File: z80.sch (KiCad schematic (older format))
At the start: 6 parts, among them P1 CONN_01X04, U1001 Z8400, U1002 AT28C64B, U1003 AS6C1008, U1004 Z8420, U1005 74LS138

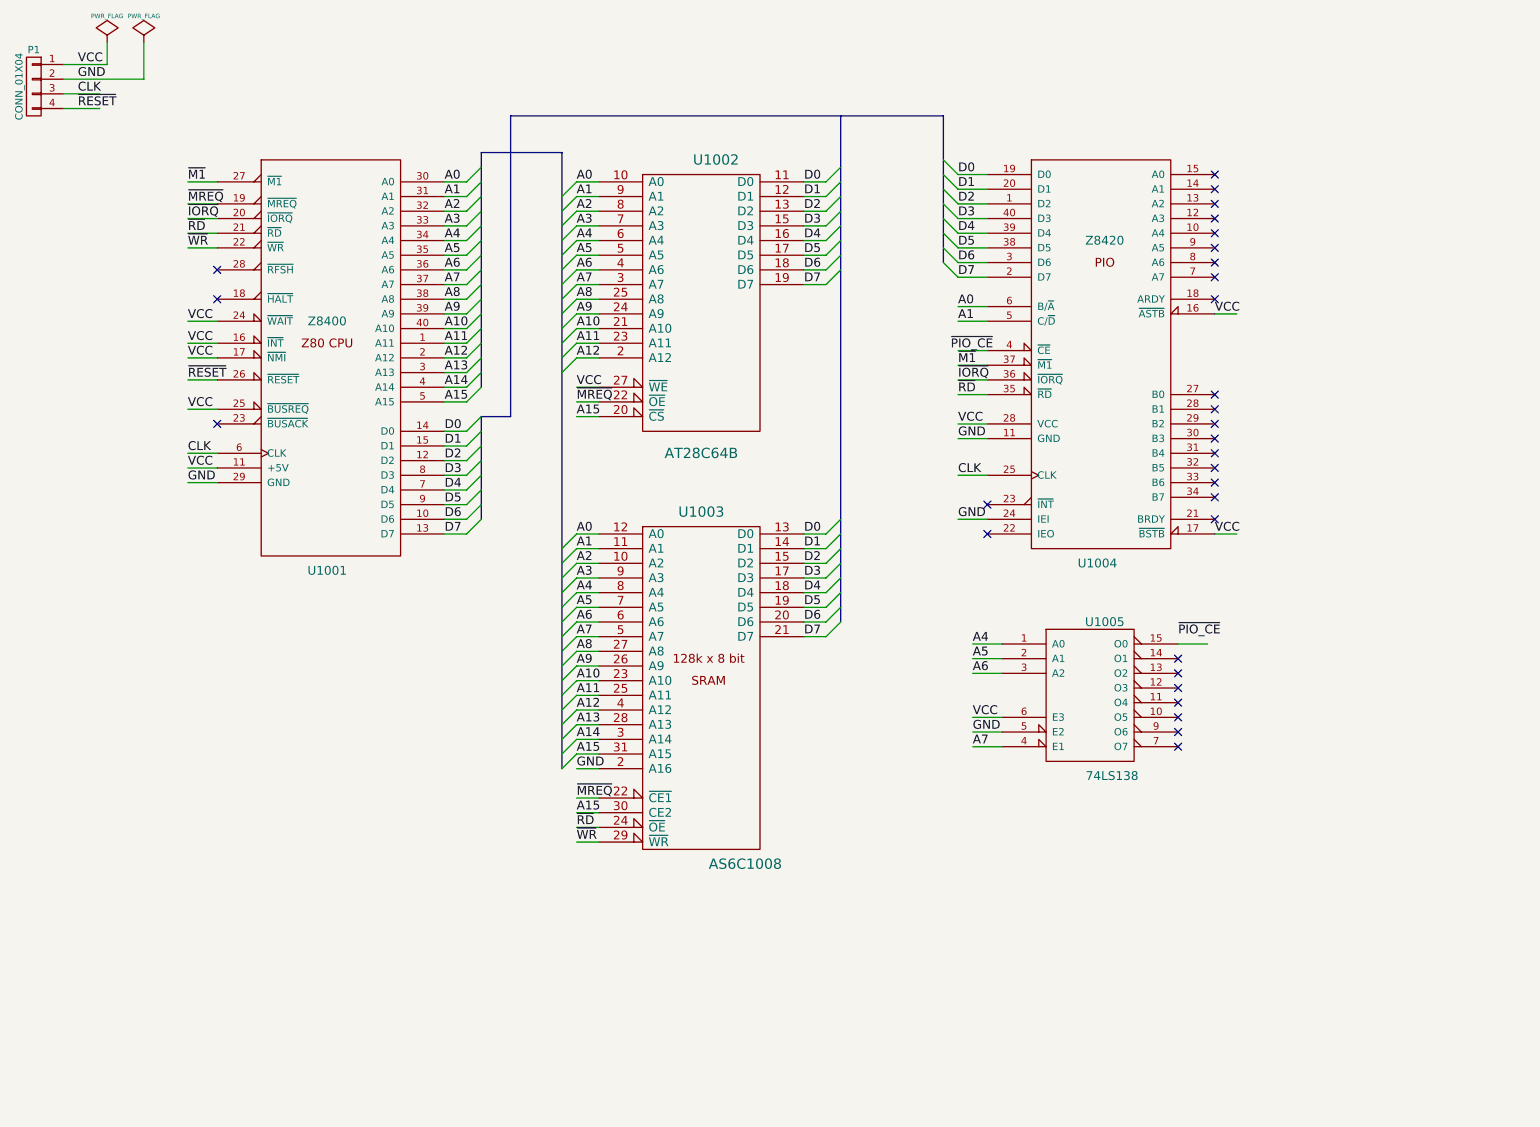
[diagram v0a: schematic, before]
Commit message: Connect ~RESET to the PIO
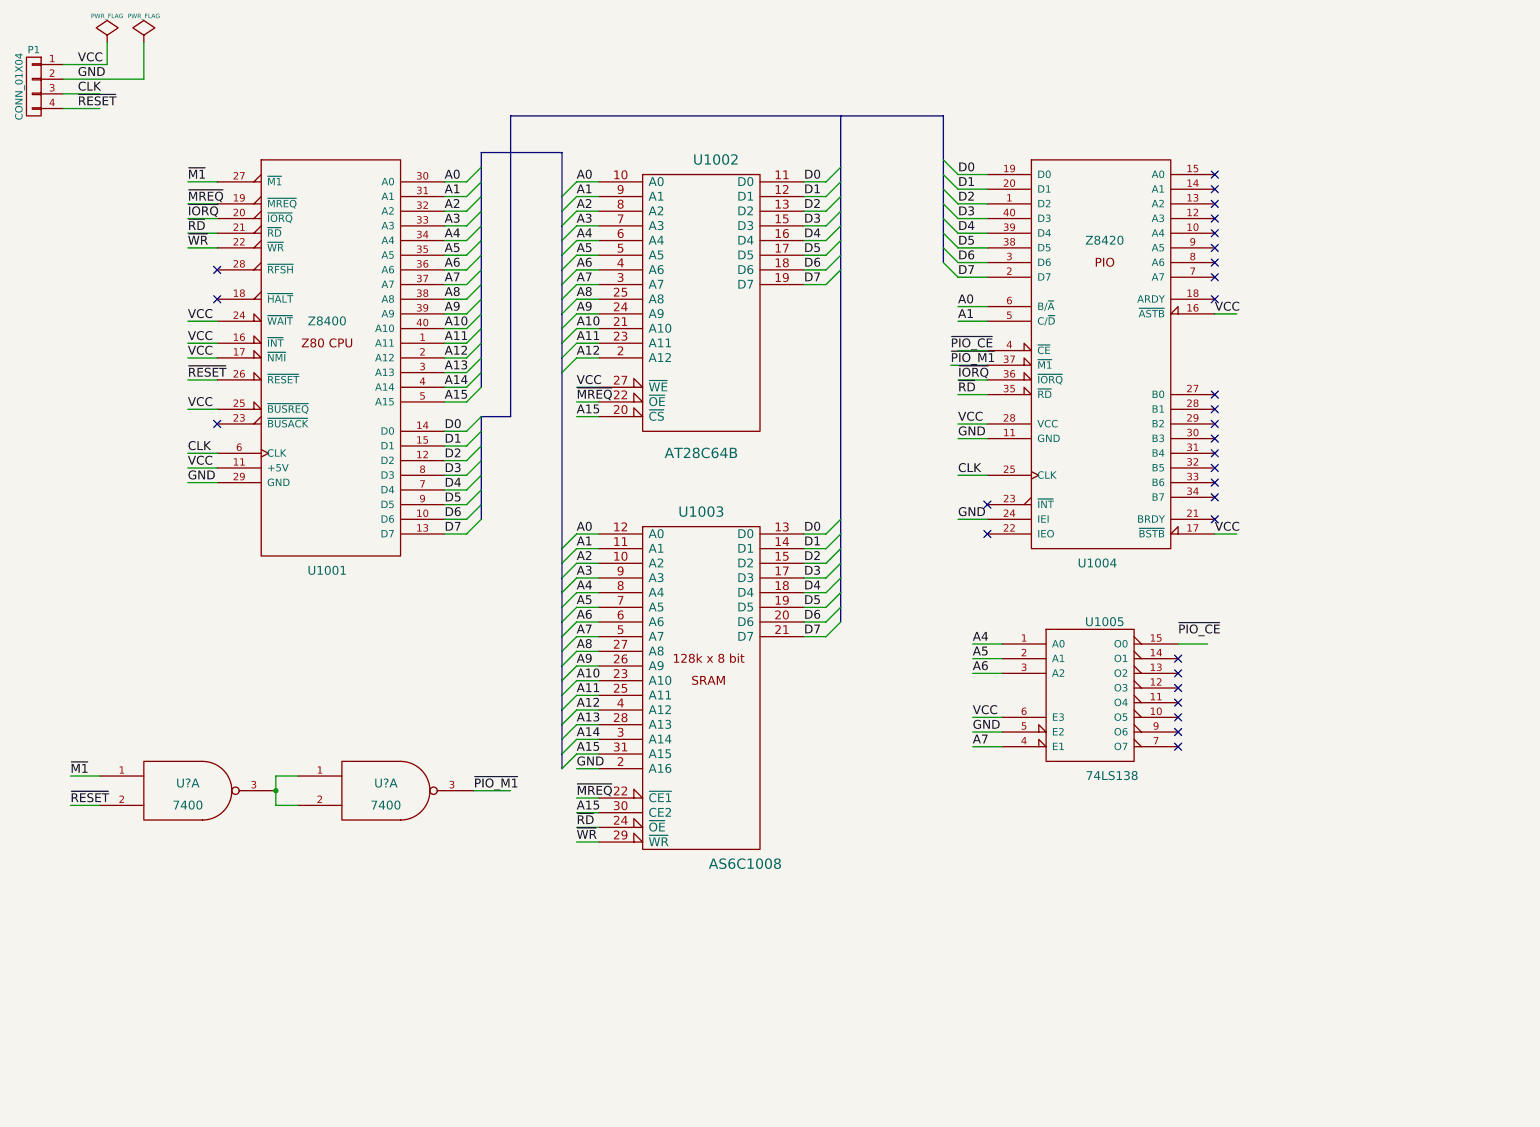
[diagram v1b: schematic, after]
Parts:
- added U? (x2): 7400, symbol 7400
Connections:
- net labels added: ~PIO_M1
- wire segments 123 -> 130
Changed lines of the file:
@@
 Text Label 4500 3100 0    60   ~ 0
 VCC
-Text Label 7100 2950 0    60   ~ 0
-~M1
+Text Label 7050 2950 0    60   ~ 0
+~PIO_M1
 Text Label 4500 3300 0    60   ~ 0
 A15
@@
 	3600 4100 3750 4100
 Wire Bus Line
-	3850 1500 3850 3100
+	3850 1500 3850 1600
+Wire Bus Line
+	3850 1600 3850 1700
+Wire Bus Line
+	3850 1700 3850 1800
+Wire Bus Line
+	3850 1800 3850 1900
+Wire Bus Line
+	3850 1900 3850 2000
+Wire Bus Line
+	3850 2000 3850 2100
+Wire Bus Line
+	3850 2100 3850 2200
+Wire Bus Line
+	3850 2200 3850 2300
+Wire Bus Line
+	3850 2300 3850 2400
+Wire Bus Line
+	3850 2400 3850 2500
+Wire Bus Line
+	3850 2500 3850 2600
+Wire Bus Line
+	3850 2600 3850 2700
+Wire Bus Line
+	3850 2700 3850 2800
+Wire Bus Line
+	3850 2800 3850 2900
+Wire Bus Line
+	3850 2900 3850 3000
+Wire Bus Line
+	3850 3000 3850 3100
 Wire Bus Line
 	3850 1500 4400 1500
@@
 	4650 5600 4500 5600
 Wire Bus Line
-	4400 1500 4400 5700
-Wire Bus Line
-	6300 1250 6300 4700
-Wire Wire Line
-	7100 2950 7300 2950
+	4400 1500 4400 1800
+Wire Bus Line
+	4400 1800 4400 1900
+Wire Bus Line
+	4400 1900 4400 2000
+Wire Bus Line
+	4400 2000 4400 2100
+Wire Bus Line
+	4400 2100 4400 2200
+Wire Bus Line
+	4400 2200 4400 2300
+Wire Bus Line
+	4400 2300 4400 2400
+Wire Bus Line
+	4400 2400 4400 2500
+Wire Bus Line
+	4400 2500 4400 2600
+Wire Bus Line
+	4400 2600 4400 2700
+Wire Bus Line
+	4400 2700 4400 2800
+Wire Bus Line
+	4400 2800 4400 2900
+Wire Bus Line
+	4400 2900 4400 3000
+Wire Bus Line
+	4400 3000 4400 4200
+Wire Bus Line
+	4400 4200 4400 4300
+Wire Bus Line
+	4400 4300 4400 4400
+Wire Bus Line
+	4400 4400 4400 4500
+Wire Bus Line
+	4400 4500 4400 4600
+Wire Bus Line
+	4400 4600 4400 4700
+Wire Bus Line
+	4400 4700 4400 4800
+Wire Bus Line
+	4400 4800 4400 4900
+Wire Bus Line
+	4400 4900 4400 5000
+Wire Bus Line
+	4400 5000 4400 5100
+Wire Bus Line
+	4400 5100 4400 5200
+Wire Bus Line
+	4400 5200 4400 5300
+Wire Bus Line
+	4400 5300 4400 5400
+Wire Bus Line
+	4400 5400 4400 5500
+Wire Bus Line
+	4400 5500 4400 5600
+Wire Bus Line
+	4400 5600 4400 5700
+Wire Bus Line
+	6300 1250 6300 1600
+Wire Bus Line
+	6300 1600 6300 1700
+Wire Bus Line
+	6300 1700 6300 1800
+Wire Bus Line
+	6300 1800 6300 1900
+Wire Bus Line
+	6300 1900 6300 2000
+Wire Bus Line
+	6300 2000 6300 2100
+Wire Bus Line
+	6300 2100 6300 2200
+Wire Bus Line
+	6300 2200 6300 2300
+Wire Bus Line
+	6300 2300 6300 4000
+Wire Bus Line
+	6300 4000 6300 4100
+Wire Bus Line
+	6300 4100 6300 4200
+Wire Bus Line
+	6300 4200 6300 4300
+Wire Bus Line
+	6300 4300 6300 4400
+Wire Bus Line
+	6300 4400 6300 4500
+Wire Bus Line
+	6300 4500 6300 4600
+Wire Bus Line
+	6300 4600 6300 4700
+Wire Wire Line
+	7050 2950 7300 2950
 Wire Wire Line
 	7100 3050 7300 3050
@@
 	7300 2350 7100 2350
 Wire Bus Line
-	7000 1250 7000 2250
+	7000 1250 7000 1550
+Wire Bus Line
+	7000 1550 7000 1650
+Wire Bus Line
+	7000 1650 7000 1750
+Wire Bus Line
+	7000 1750 7000 1850
+Wire Bus Line
+	7000 1850 7000 1950
+Wire Bus Line
+	7000 1950 7000 2050
+Wire Bus Line
+	7000 2050 7000 2150
+Wire Bus Line
+	7000 2150 7000 2250
 Wire Wire Line
 	1000 900  1300 900
@@
 	1850 3050 2050 3050
 Wire Bus Line
-	3850 4000 3850 3300
+	3850 3300 3850 3400
+Wire Bus Line
+	3850 3400 3850 3500
+Wire Bus Line
+	3850 3500 3850 3600
+Wire Bus Line
+	3850 3600 3850 3700
+Wire Bus Line
+	3850 3700 3850 3800
+Wire Bus Line
+	3850 3800 3850 3900
+Wire Bus Line
+	3850 3900 3850 4000
 Wire Bus Line
 	3850 3300 4050 3300
@@
 Text Label 4500 5700 0    60   ~ 0
 GND
+$Comp
+L 7400 U?
+U 1 1 5503FD72
+P 1850 5850
+F 0 "U?" H 1850 5900 60  0000 C CNN
+F 1 "7400" H 1850 5750 60  0000 C CNN
+F 2 "" H 1850 5850 60  0000 C CNN
+F 3 "" H 1850 5850 60  0000 C CNN
+	1    1850 5850
+	1    0    0    -1
+$EndComp
+$Comp
+L 7400 U?
+U 1 1 5503FD9E
+P 3200 5850
+F 0 "U?" H 3200 5900 60  0000 C CNN
+F 1 "7400" H 3200 5750 60  0000 C CNN
+F 2 "" H 3200 5850 60  0000 C CNN
+F 3 "" H 3200 5850 60  0000 C CNN
+	1    3200 5850
+	1    0    0    -1
+$EndComp
+Wire Wire Line
+	2450 5750 2450 5850
+Wire Wire Line
+	2450 5850 2450 5950
+Wire Wire Line
+	2450 5750 2600 5750
+Wire Wire Line
+	2450 5950 2600 5950
+Connection ~ 2450 5850
+Wire Wire Line
+	1050 5750 1250 5750
+Text Label 1050 5750 0    60   ~ 0
+~M1
+Wire Wire Line
+	1050 5950 1250 5950
+Text Label 1050 5950 0    60   ~ 0
+~RESET
+Wire Wire Line
+	3800 5850 4050 5850
+Text Label 3800 5850 0    60   ~ 0
+~PIO_M1
 $EndSCHEMATC

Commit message: Add PIO port A connector and 40 pin bus connector
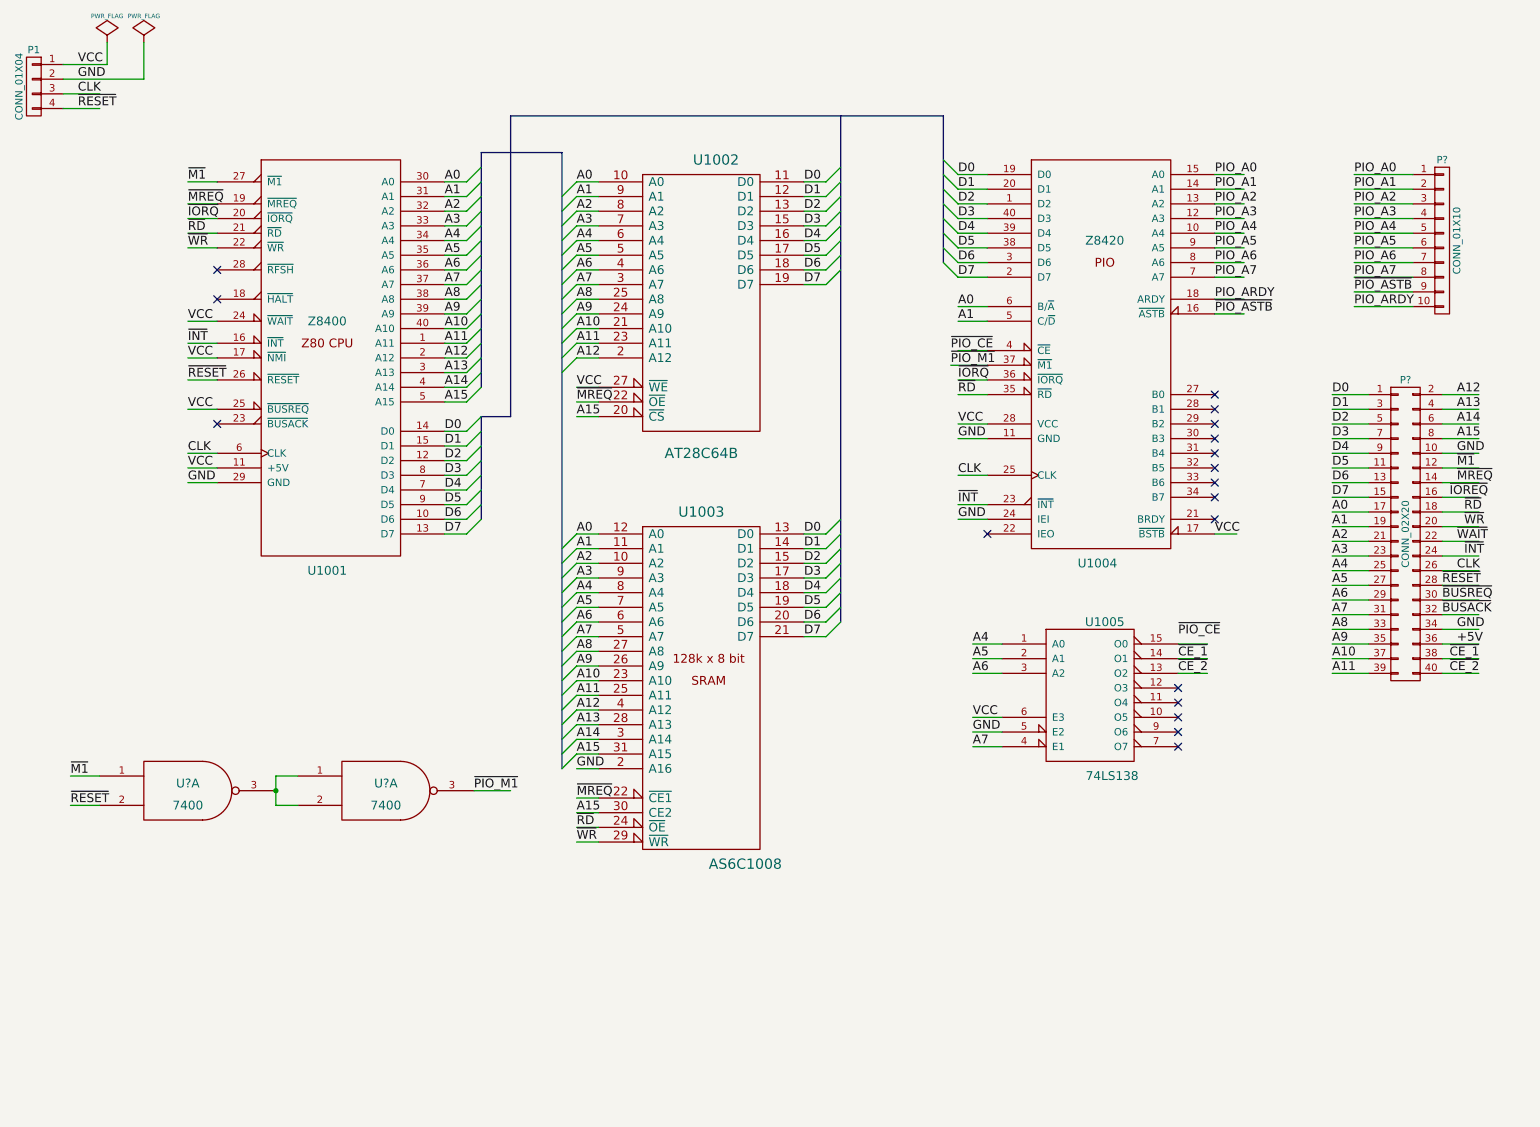
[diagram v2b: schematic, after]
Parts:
- added P?: CONN_01X10, symbol CONN_01X10
- added P?: CONN_02X20, symbol CONN_02X20
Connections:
- net labels added: +5V, PIO_A0, PIO_A1, PIO_A2, PIO_A3, PIO_A4, PIO_A5, PIO_A6, PIO_A7, PIO_ARDY, ~BUSACK, ~BUSREQ, ~CE_1, ~CE_2, ~INT, ~IOREQ, ~PIO_ASTB, ~WAIT
- wire segments 130 -> 191
- no-connect marks 30 -> 18

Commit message: Commit before removing tracks
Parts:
- gave numbers to parts that had none: 3
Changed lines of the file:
@@
 	4050 1250 7000 1250
 $Comp
-L PWR_FLAG #FLG01
+L PWR_FLAG #FLG1
 U 1 1 54F097BB
 P 1300 750
-F 0 "#FLG01" H 1300 845 30  0001 C CNN
+F 0 "#FLG1" H 1300 845 30  0001 C CNN
 F 1 "PWR_FLAG" H 1300 930 30  0000 C CNN
 F 2 "" H 1300 750 60  0000 C CNN
@@
 $EndComp
 $Comp
-L PWR_FLAG #FLG02
+L PWR_FLAG #FLG2
 U 1 1 54F097DB
 P 1550 750
-F 0 "#FLG02" H 1550 845 30  0001 C CNN
+F 0 "#FLG2" H 1550 845 30  0001 C CNN
 F 1 "PWR_FLAG" H 1550 930 30  0000 C CNN
 F 2 "" H 1550 750 60  0000 C CNN
@@
 GND
 $Comp
-L 7400 U?
+L 7400 U1
 U 1 1 5503FD72
 P 1850 5850
-F 0 "U?" H 1850 5900 60  0000 C CNN
+F 0 "U1" H 1850 5900 60  0000 C CNN
 F 1 "7400" H 1850 5750 60  0000 C CNN
 F 2 "" H 1850 5850 60  0000 C CNN
@@
 $EndComp
 $Comp
-L 7400 U?
-U 1 1 5503FD9E
+L 7400 U1
+U 2 1 5503FD9E
 P 3200 5850
-F 0 "U?" H 3200 5900 60  0000 C CNN
+F 0 "U1" H 3200 5900 60  0000 C CNN
 F 1 "7400" H 3200 5750 60  0000 C CNN
 F 2 "" H 3200 5850 60  0000 C CNN
 F 3 "" H 3200 5850 60  0000 C CNN
-	1    3200 5850
+	2    3200 5850
 	1    0    0    -1
 $EndComp
@@
 ~PIO_M1
 $Comp
-L CONN_01X10 P?
+L CONN_01X10 P3
 U 1 1 55045F71
 P 10400 2100
-F 0 "P?" H 10400 2650 50  0000 C CNN
+F 0 "P3" H 10400 2650 50  0000 C CNN
 F 1 "CONN_01X10" V 10500 2100 50  0000 C CNN
 F 2 "" H 10400 2100 60  0000 C CNN
@@
 ~INT
 $Comp
-L CONN_02X20 P?
+L CONN_02X20 P2
 U 1 1 55046C1D
 P 10150 4100
-F 0 "P?" H 10150 5150 50  0000 C CNN
+F 0 "P2" H 10150 5150 50  0000 C CNN
 F 1 "CONN_02X20" V 10150 4100 50  0000 C CNN
 F 2 "" H 10150 3150 60  0000 C CNN
